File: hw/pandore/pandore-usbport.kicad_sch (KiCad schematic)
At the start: 0 parts

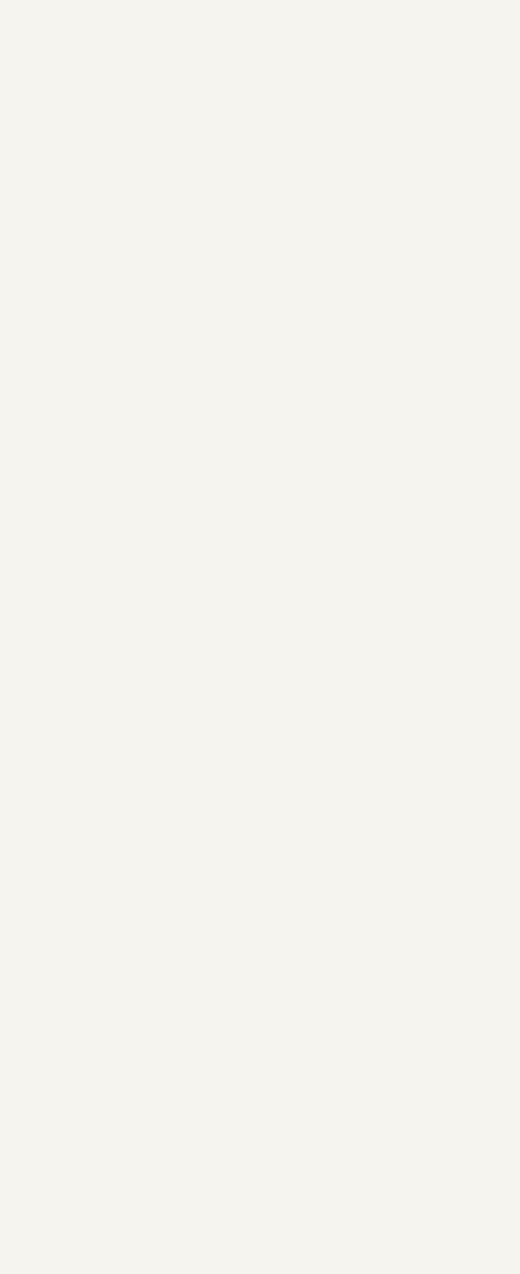
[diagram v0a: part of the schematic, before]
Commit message: added usb, hdmi and combo xlrtrs connectors resized pcb for something realistic (still wip)
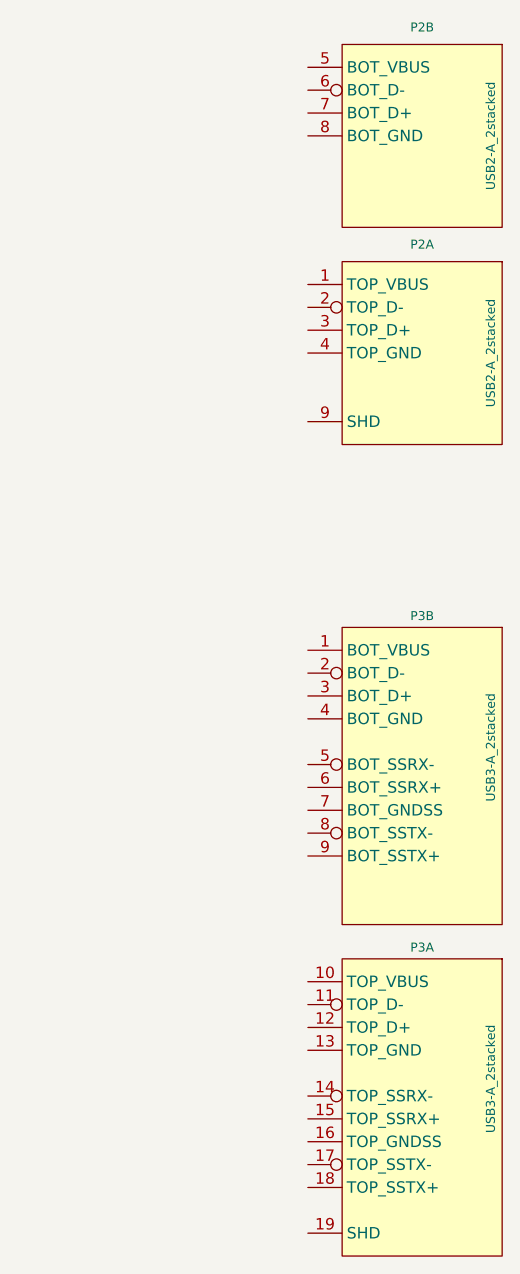
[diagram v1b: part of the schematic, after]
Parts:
- added P2: USB2-A_2stacked, reekilib_con:USB2_A_RCPT_HORZ_2STACKED, symbol reekilib_con:USB2-A_2stacked
- added P3: USB3-A_2stacked, reekilib_con:USB3_A_RCPT_HORZ_2STACKED, symbol reekilib_con:USB3-A_2stacked

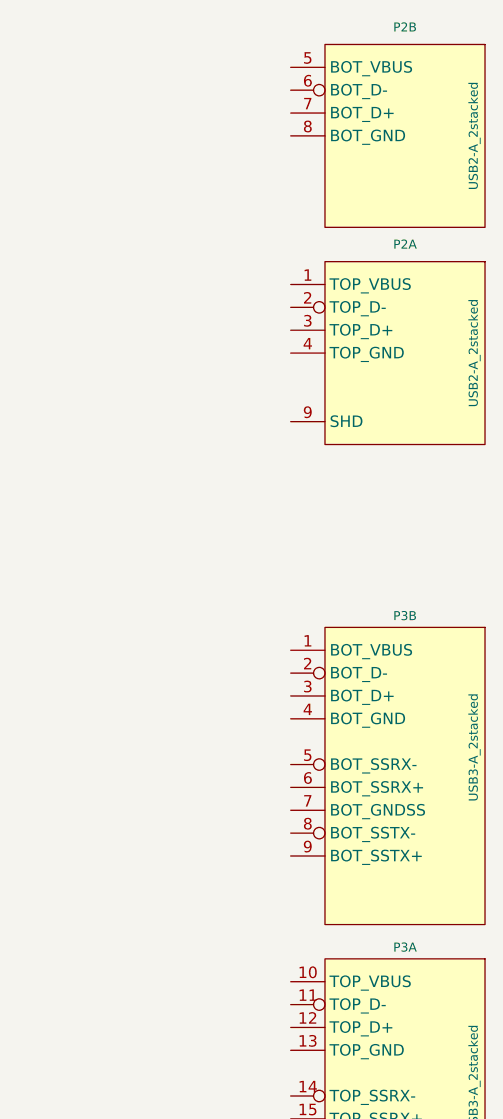
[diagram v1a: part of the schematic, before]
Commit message: added all remaining connectors (only missing M.2 now)
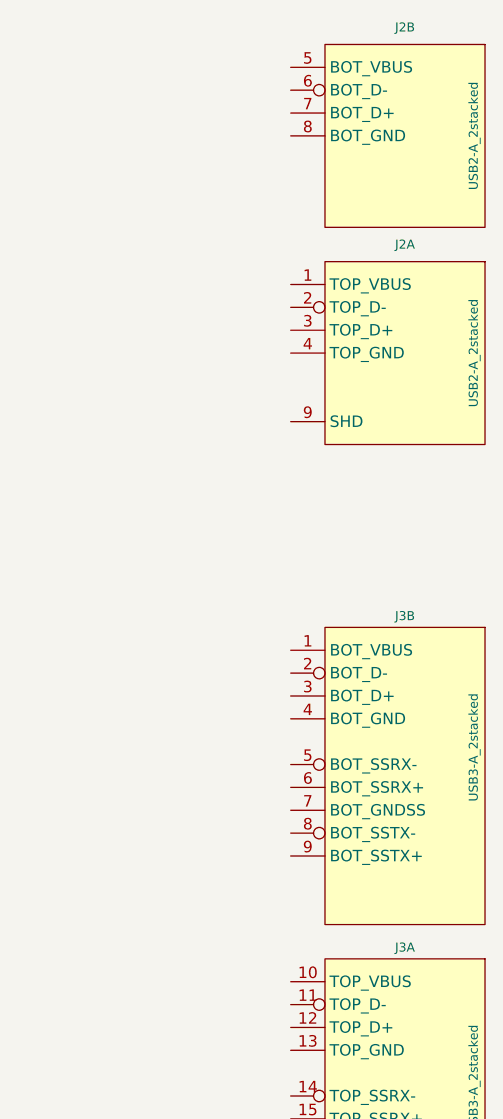
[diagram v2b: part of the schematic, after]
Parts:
- J3: renamed from P3; Imax (none) -> 1.5A; Vmax (none) -> 30V
- renumbered P2 to J2
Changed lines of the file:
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@@
 		(dnp no)
 		(fields_autoplaced yes)
-		(property "Reference" "P3"
+		(property "Reference" "J3"
 			(at 266.7 86.36 0)
 			(do_not_autoplace yes)
@@
 				)
 				(justify left)
+				(hide yes)
+			)
+		)
+		(property "Vmax" "30V"
+			(at 272.415 127 0)
+			(effects
+				(font
+					(size 0.9906 0.9906)
+				)
+				(hide yes)
+			)
+		)
+		(property "Imax" "1.5A"
+			(at 266.7 127 0)
+			(effects
+				(font
+					(size 0.9906 0.9906)
+				)
 				(hide yes)
 			)
@@
 			(project ""
 				(path "/e55f2700-f75a-4062-8a27-fe258faa8966/bb2b2e05-965b-41e8-90ff-dc0d1c46f97c"
-					(reference "P3")
+					(reference "J3")
 					(unit 2)
 				)
@@
 		(dnp no)
 		(fields_autoplaced yes)
-		(property "Reference" "P2"
+		(property "Reference" "J2"
 			(at 266.7 20.955 0)
 			(do_not_autoplace yes)
@@
 			(project ""
 				(path "/e55f2700-f75a-4062-8a27-fe258faa8966/bb2b2e05-965b-41e8-90ff-dc0d1c46f97c"
-					(reference "P2")
+					(reference "J2")
 					(unit 2)
 				)
@@
 		(dnp no)
 		(fields_autoplaced yes)
-		(property "Reference" "P2"
+		(property "Reference" "J2"
 			(at 266.7 45.085 0)
 			(do_not_autoplace yes)
@@
 			(project ""
 				(path "/e55f2700-f75a-4062-8a27-fe258faa8966/bb2b2e05-965b-41e8-90ff-dc0d1c46f97c"
-					(reference "P2")
+					(reference "J2")
 					(unit 1)
 				)
@@
 		(dnp no)
 		(fields_autoplaced yes)
-		(property "Reference" "P3"
+		(property "Reference" "J3"
 			(at 266.7 123.19 0)
 			(do_not_autoplace yes)
@@
 				)
 				(justify left)
+				(hide yes)
+			)
+		)
+		(property "Vmax" "30V"
+			(at 272.415 163.83 0)
+			(effects
+				(font
+					(size 0.9906 0.9906)
+				)
+				(hide yes)
+			)
+		)
+		(property "Imax" "1.5A"
+			(at 266.7 163.83 0)
+			(effects
+				(font
+					(size 0.9906 0.9906)
+				)
 				(hide yes)
 			)
@@
 			(project ""
 				(path "/e55f2700-f75a-4062-8a27-fe258faa8966/bb2b2e05-965b-41e8-90ff-dc0d1c46f97c"
-					(reference "P3")
+					(reference "J3")
 					(unit 1)
 				)

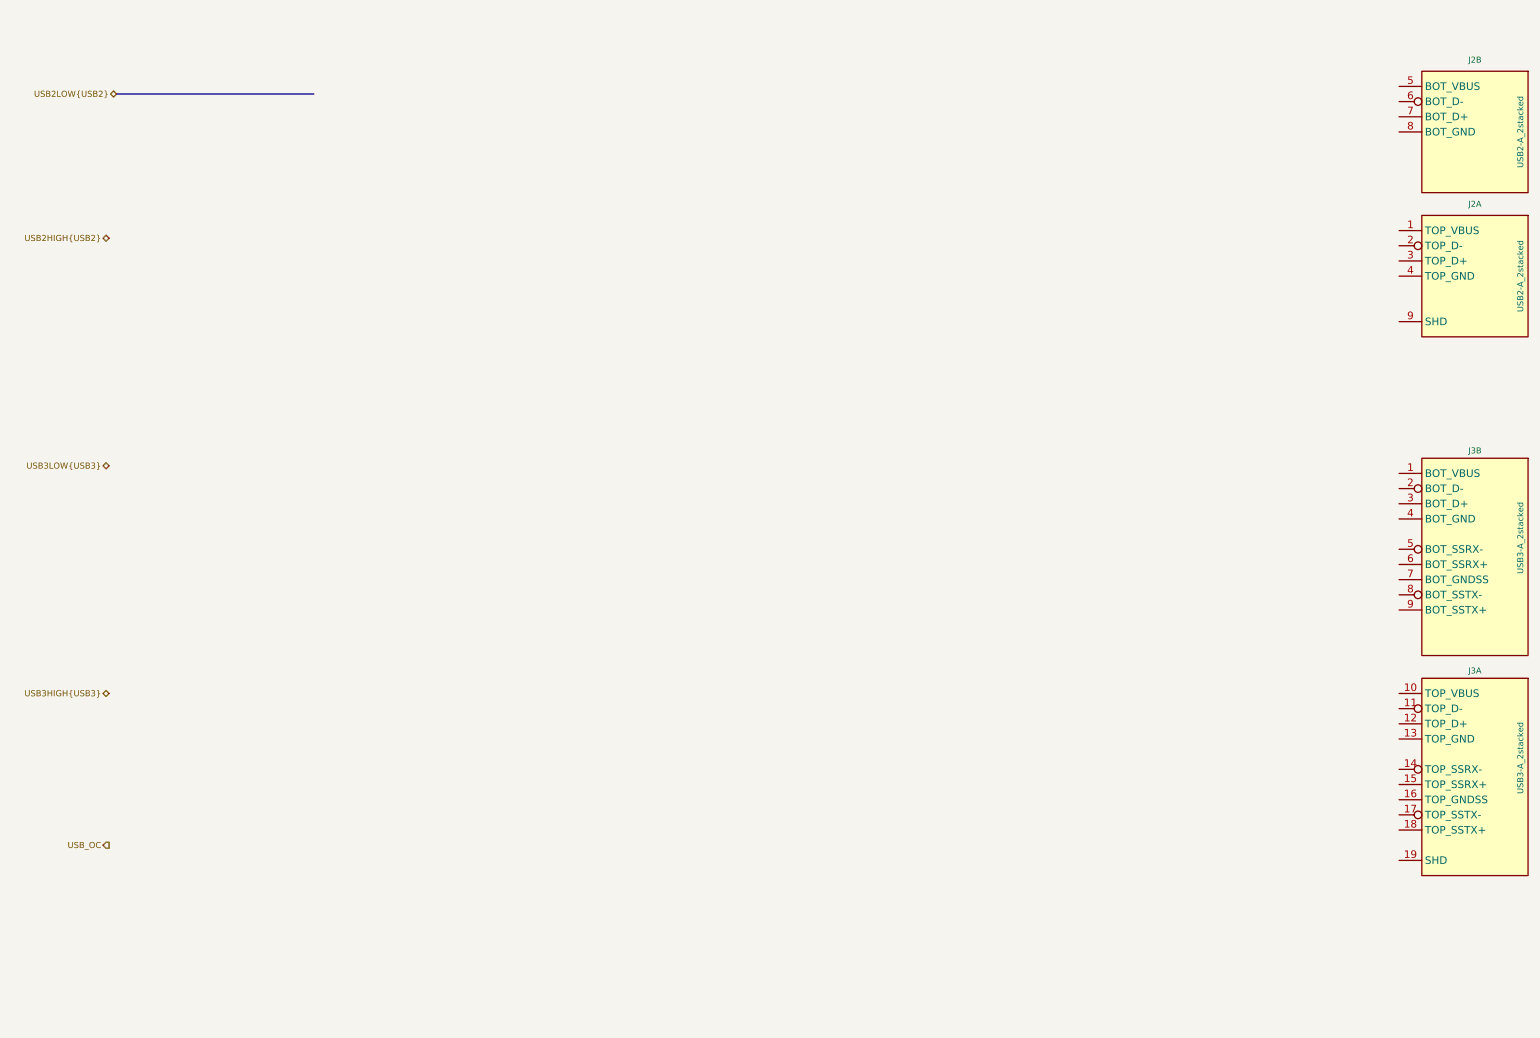
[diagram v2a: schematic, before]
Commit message: Added lots to sch and pcb: eth passive, audio codec, midi, teensy Corrected and added support for M.2
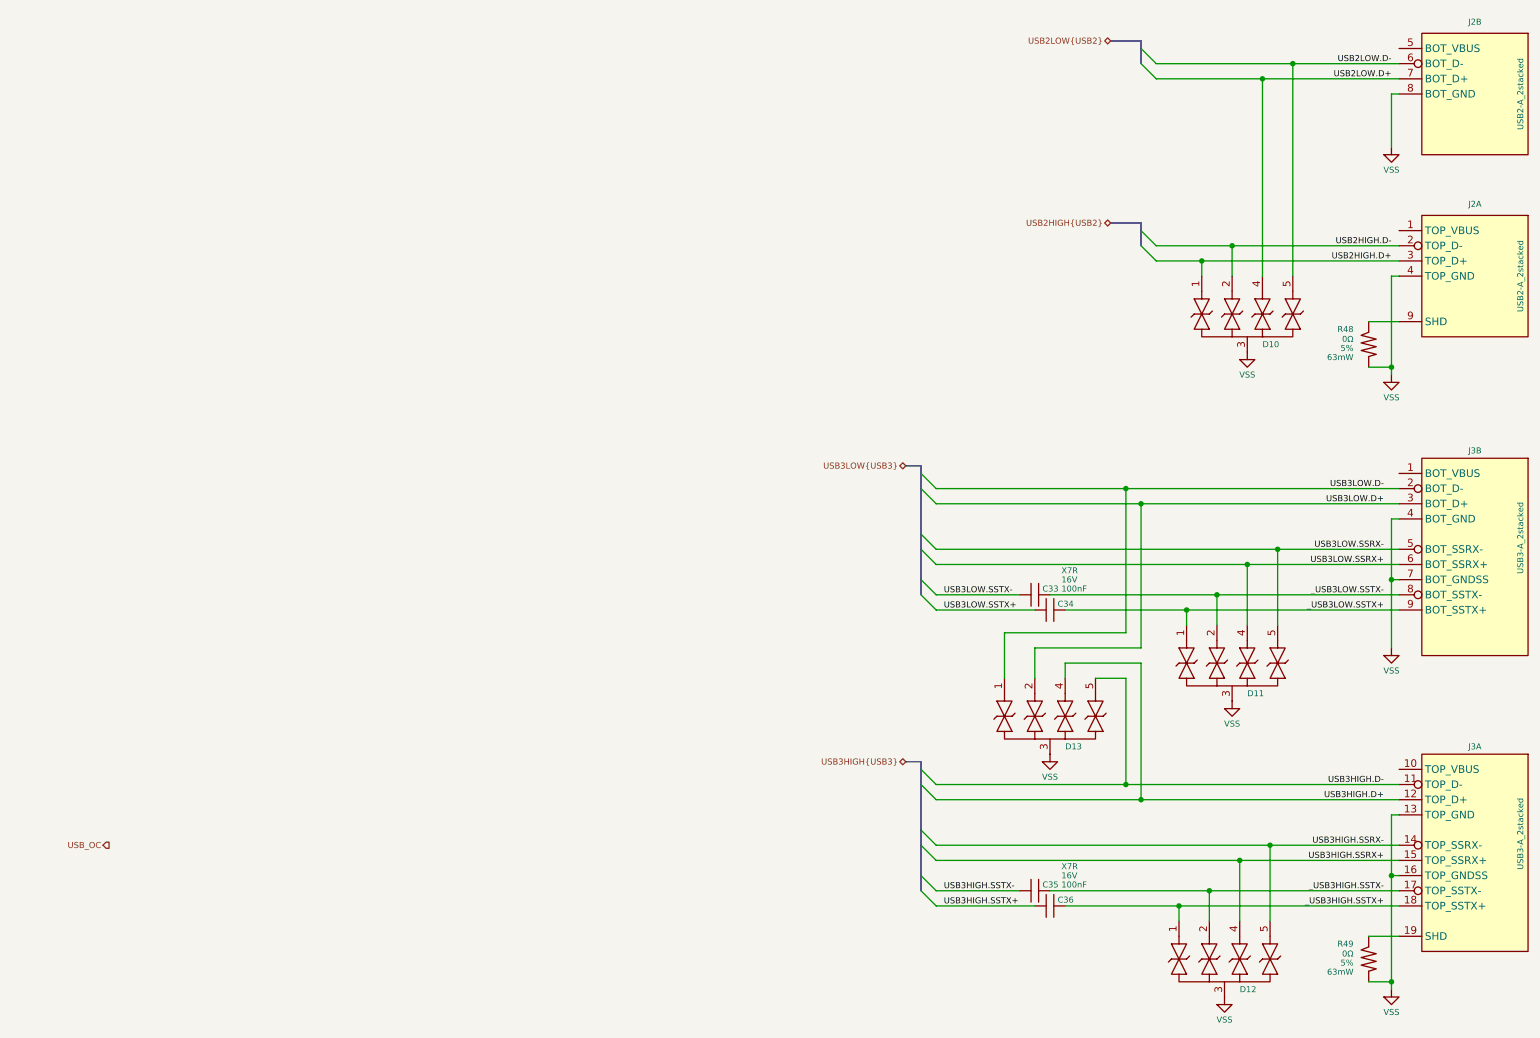
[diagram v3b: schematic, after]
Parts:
- added C33, C34, C35, C36: ${Capacitance}, ${Voltage}, ${Dielectric}, reekilib_cap:CAPC1005, symbol reekilib_cap:cap
- added D10, D11, D12, D13: ${Vbr}, reekilib_dfn:DFN50P100X250X55-10, symbol reekilib_tvs:diode_tvsbi_4
- added R48, R49: ${Resistance}, ${Tolerance}, ${Power}, reekilib_res:RESC1005, symbol reekilib_res:res
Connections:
- net USB3LOW.D-: now reaches J3.2 (BOT_D-)
- net USB3LOW.D-: now also D13.1
- net USB3LOW.D+: now reaches J3.3 (BOT_D+)
- net USB3LOW.D+: now also D13.2
- net VSS: now reaches J3.4 (BOT_GND)
- net VSS: now also J2.4 (TOP_GND), J2.8 (BOT_GND), J3.13 (TOP_GND), J3.16 (TOP_GNDSS), J3.7 (BOT_GNDSS), D10.3, D11.3, D12.3, D13.3, R48.1, R49.1
- net USB3LOW.SSRX-: now reaches J3.5 (BOT_SSRX-)
- net USB3LOW.SSRX-: now also D11.5
- net USB3LOW.SSRX+: now reaches J3.6 (BOT_SSRX+)
- net USB3LOW.SSRX+: now also D11.4
- net _USB3LOW.SSTX-: now reaches J3.8 (BOT_SSTX-)
- net _USB3LOW.SSTX-: now also C33.1, D11.2
- net _USB3LOW.SSTX+: now reaches J3.9 (BOT_SSTX+)
- net _USB3LOW.SSTX+: now also C34.1, D11.1
- net USB2LOW.D-: now reaches J2.6 (BOT_D-)
- net USB2LOW.D-: now also D10.5
- net USB2LOW.D+: now reaches J2.7 (BOT_D+)
- net USB2LOW.D+: now also D10.4
- net USB2HIGH.D-: now reaches J2.2 (TOP_D-)
- net USB2HIGH.D-: now also D10.2
- net USB2HIGH.D+: now reaches J2.3 (TOP_D+)
- net USB2HIGH.D+: now also D10.1
- net at J2.9 (SHD): now also R48.2
- net USB3HIGH.D-: now reaches J3.11 (TOP_D-)
- net USB3HIGH.D-: now also D13.5
- net USB3HIGH.D+: now reaches J3.12 (TOP_D+)
- net USB3HIGH.D+: now also D13.4
- net USB3HIGH.SSRX-: now reaches J3.14 (TOP_SSRX-)
- net USB3HIGH.SSRX-: now also D12.5
- net USB3HIGH.SSRX+: now reaches J3.15 (TOP_SSRX+)
- net USB3HIGH.SSRX+: now also D12.4
- net _USB3HIGH.SSTX-: now reaches J3.17 (TOP_SSTX-)
- net _USB3HIGH.SSTX-: now also C35.1, D12.2
- net _USB3HIGH.SSTX+: now reaches J3.18 (TOP_SSTX+)
- net _USB3HIGH.SSTX+: now also C36.1, D12.1
- net at J3.19 (SHD): now also R49.2
- new net USB3HIGH.SSTX+: C36.2
- new net USB3HIGH.SSTX-: C35.2
- new net USB3LOW.SSTX+: C34.2
- new net USB3LOW.SSTX-: C33.2
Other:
- moved on the sheet: J2B, J3A

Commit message: Lots of routing done power blocks intra-routing mostly done rp2350 routing mostly done some label cleanup
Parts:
- D10, D11, D12, D13: footprint reekilib_dfn:DFN50P100X250X55-10 -> reekilib_dfn:DFN50P100X250X55-10_ESD204
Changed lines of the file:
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@@
 			)
 		)
-		(property "Footprint" "reekilib_dfn:DFN50P100X250X55-10"
+		(property "Footprint" "reekilib_dfn:DFN50P100X250X55-10_ESD204"
 			(at 226.06 138.43 0)
 			(do_not_autoplace yes)
@@
 			)
 		)
-		(property "Footprint" "reekilib_dfn:DFN50P100X250X55-10"
+		(property "Footprint" "reekilib_dfn:DFN50P100X250X55-10_ESD204"
 			(at 195.58 147.32 0)
 			(do_not_autoplace yes)
@@
 			)
 		)
-		(property "Footprint" "reekilib_dfn:DFN50P100X250X55-10"
+		(property "Footprint" "reekilib_dfn:DFN50P100X250X55-10_ESD204"
 			(at 228.6 80.01 0)
 			(do_not_autoplace yes)
@@
 			)
 		)
-		(property "Footprint" "reekilib_dfn:DFN50P100X250X55-10"
+		(property "Footprint" "reekilib_dfn:DFN50P100X250X55-10_ESD204"
 			(at 224.79 187.96 0)
 			(do_not_autoplace yes)
